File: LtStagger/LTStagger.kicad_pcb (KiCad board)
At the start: 2 copper layers, 51 parts, among them K0 K00, K1 K01, K10 K10, K11 K11, K12 K12, K2 K02, K20 K20, K21 K21, K22 K22, K30 K30, K31 K31, K32 K32, K33 K33, K40 K40, K41 K41, K42 K42, K43 K43, K50 K50, K51 K51, K53 K53, SW1 Rotary_Encoder_Switch, U1 ProMicro, U2 TRRS, U3 MCP23018-E_SP

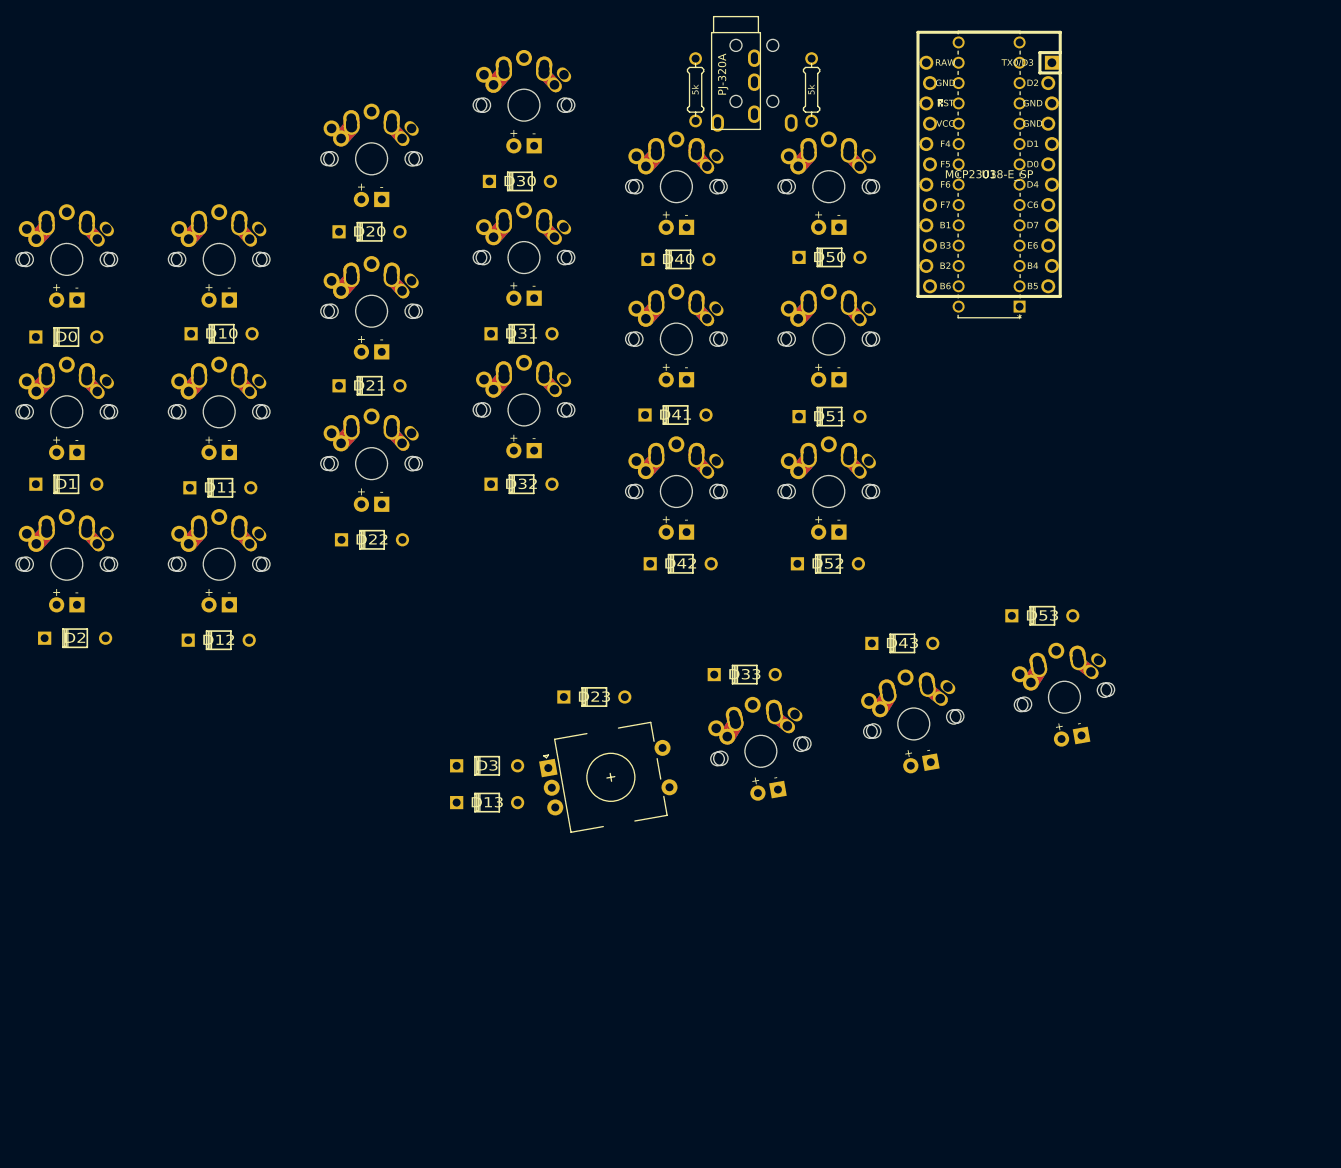
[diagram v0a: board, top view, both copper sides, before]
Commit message: About to even out the side bezels
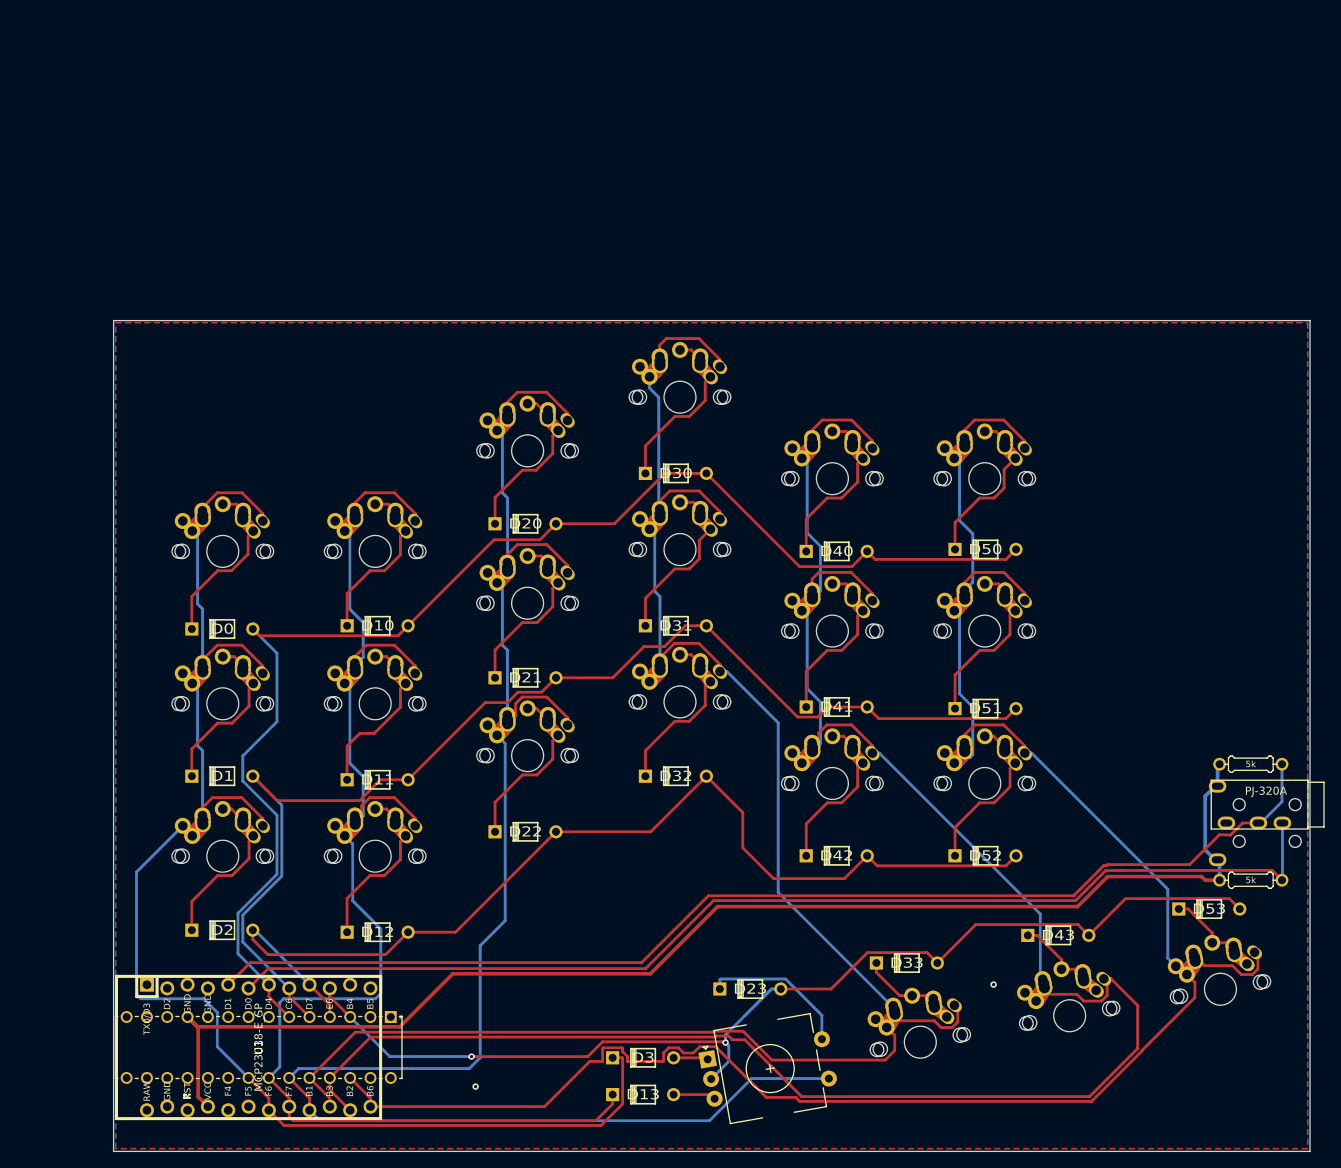
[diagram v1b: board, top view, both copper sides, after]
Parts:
- K0, K1, K10, K11, K12, K2, K20, K21, K22, K30, K31, K32, K33, K40, K41, K42, K43, K50, K51, K53, L52: footprint Keebio-Parts:Triple-Dual-1u-LED -> Digi:Triple-Dual-1u
- moved U1 142.3 mm to (81.1, 136.6), turned to 0 degrees
- moved U2 120.6 mm to (212.3, 108.5), turned to 270 degrees
- moved U3 118.6 mm to (97.7, 132.8), turned to 270 degrees
- moved R4 113.0 mm to (205.2, 115.7), turned to 180 degrees
- moved R5 109.2 mm to (205.2, 101.2), turned to 180 degrees
- moved D53 42.2 mm to (200.0, 119.3)
- moved D41 41.7 mm to (153.4, 94.0)
- moved D12 41.6 mm to (96.0, 122.2)
- moved D40 41.5 mm to (153.4, 74.6)
- moved SW1 41.5 mm to (145.1, 139.2)
- moved D52 41.5 mm to (172.0, 112.7)
- moved K33 41.5 mm to (163.8, 135.9)
- moved D11 41.5 mm to (96.0, 103.2)
- moved D10 41.4 mm to (96.0, 83.9)
- moved D20 41.4 mm to (114.5, 71.2)
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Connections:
- U1 pad 1: Net-(U1-Pad1) -> (no net)
- U1 pad 10: Row2 -> Row3
- U1 pad 11: Net-(U1-Pad11) -> (no net)
- U1 pad 12: Net-(U1-Pad12) -> (no net)
- U1 pad 19: Net-(U1-Pad19) -> (no net)
- U1 pad 2: Net-(U1-Pad2) -> (no net)
- U1 pad 20: Net-(U1-Pad20) -> (no net)
- U1 pad 22: Net-(U1-Pad22) -> (no net)
- U1 pad 24: Net-(U1-Pad24) -> (no net)
- U1 pad 8: Net-(U1-Pad8) -> Row1
- U1 pad 9: Row1 -> Row2
- U3 pad 10: Net-(U3-Pad10) -> (no net)
- U3 pad 12: Net-(U3-Pad12) -> (no net)
- U3 pad 13: Net-(U3-Pad13) -> (no net)
- U3 pad 14: Net-(U3-Pad14) -> (no net)
- U3 pad 15: Net-(U3-Pad15) -> (no net)
- U3 pad 16: Net-(U3-Pad16) -> (no net)
- U3 pad 17: Net-(U3-Pad17) -> (no net)
- U3 pad 18: Net-(U3-Pad18) -> (no net)
- U3 pad 19: Net-(U3-Pad19) -> (no net)
- U3 pad 2: Net-(U3-Pad2) -> (no net)
- U3 pad 20: Net-(U3-Pad20) -> (no net)
- U3 pad 27: Net-(U3-Pad27) -> (no net)
- U3 pad 28: Net-(U3-Pad28) -> (no net)
- U3 pad 3: Row2 -> Row3
- U3 pad 4: Net-(U3-Pad4) -> Row2
- U3 pad 7: Net-(U3-Pad7) -> (no net)
- U3 pad 8: Net-(U3-Pad8) -> (no net)
- U3 pad 9: Net-(U3-Pad9) -> (no net)
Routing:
- net Col4: track 0.00 -> 256.0 mm
- net Col5: track 0.00 -> 251.8 mm
- net Col3: track 0.00 -> 227.1 mm
- net Col2: track 0.00 -> 215.7 mm
- net Col0: track 0.00 -> 180.5 mm
- net Row0: track 0.00 -> 168.7 mm
- net Col1: track 0.00 -> 168.6 mm
- net VCC: track 0.00 -> 166.1 mm
- net Row1: track 0.00 -> 149.2 mm
- net SCL: track 0.00 -> 145.9 mm
- net SDA: track 0.00 -> 143.0 mm
- net Row3: track 0.00 -> 139.7 mm, vias 0 -> 2
- net Row2: track 0.00 -> 131.7 mm
- net Net-(D51-Pad2): track 0.00 -> 19.7 mm
- net Net-(D32-Pad2): track 0.00 -> 19.7 mm
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- added copper zone on B.Cu, net GND
- added copper zone on F.Cu, net GND
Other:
- board outline added: 149.6 x 103.8 mm
- net class Default: clearance 0.2 -> 0.25; trace_width 0.25 -> 0.35
- net class Power added: clearance 0.25, trace_width 0.45, via_dia 1, via_drill 0.4
- rule trace_clearance: 0.2 -> 0.25
- rule trace_min: 0.2 -> 0.3
- rule via_min_drill: 0.3 -> 0.4
- rule via_min_size: 0.4 -> 0.5
